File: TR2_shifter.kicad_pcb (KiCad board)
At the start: 2 copper layers, 40 parts, among them J1 Conn_02x07_Odd_Even, J2 Conn_02x07_Odd_Even, U1 LM393DT, U2 LM393DT, U3 LM393DT, U4 LM393DT, U5 LM393DT, U6 LM393DT, U7 LM393DT

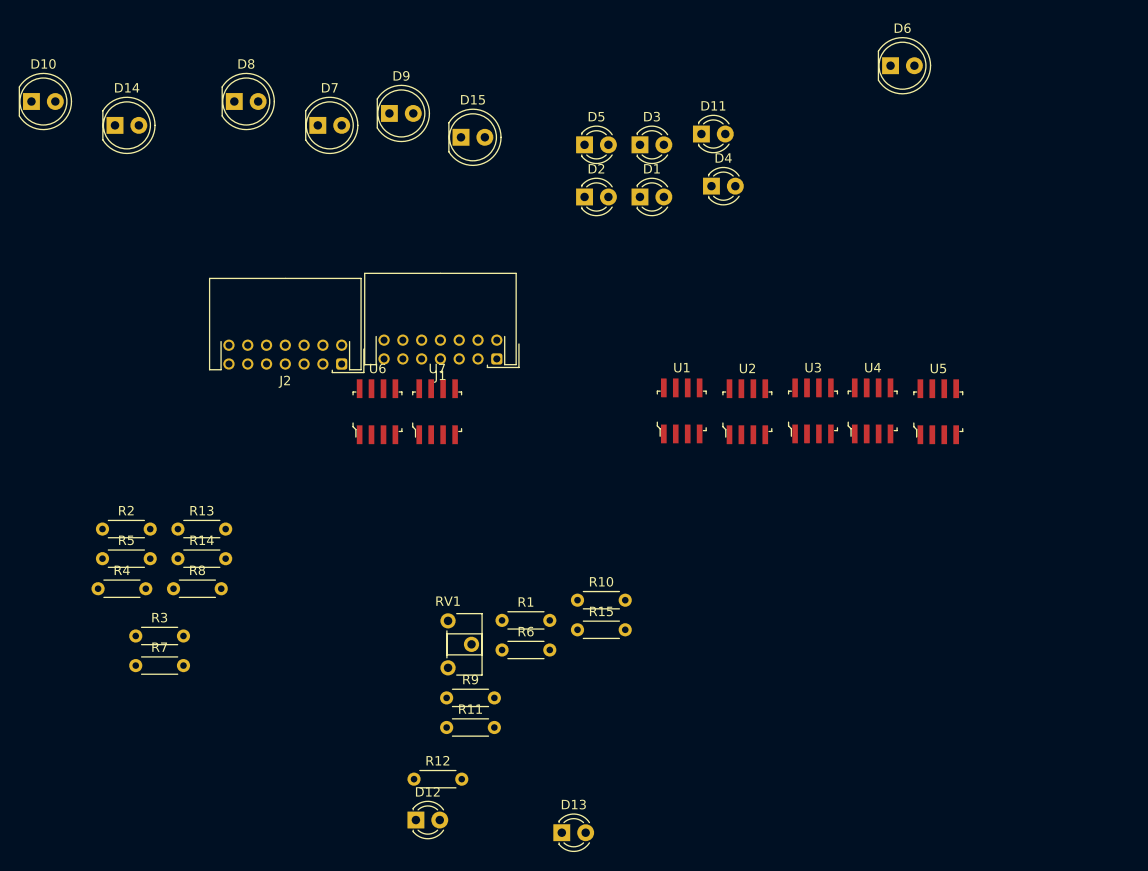
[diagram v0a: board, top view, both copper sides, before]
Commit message: First compact layout - beginning wiring
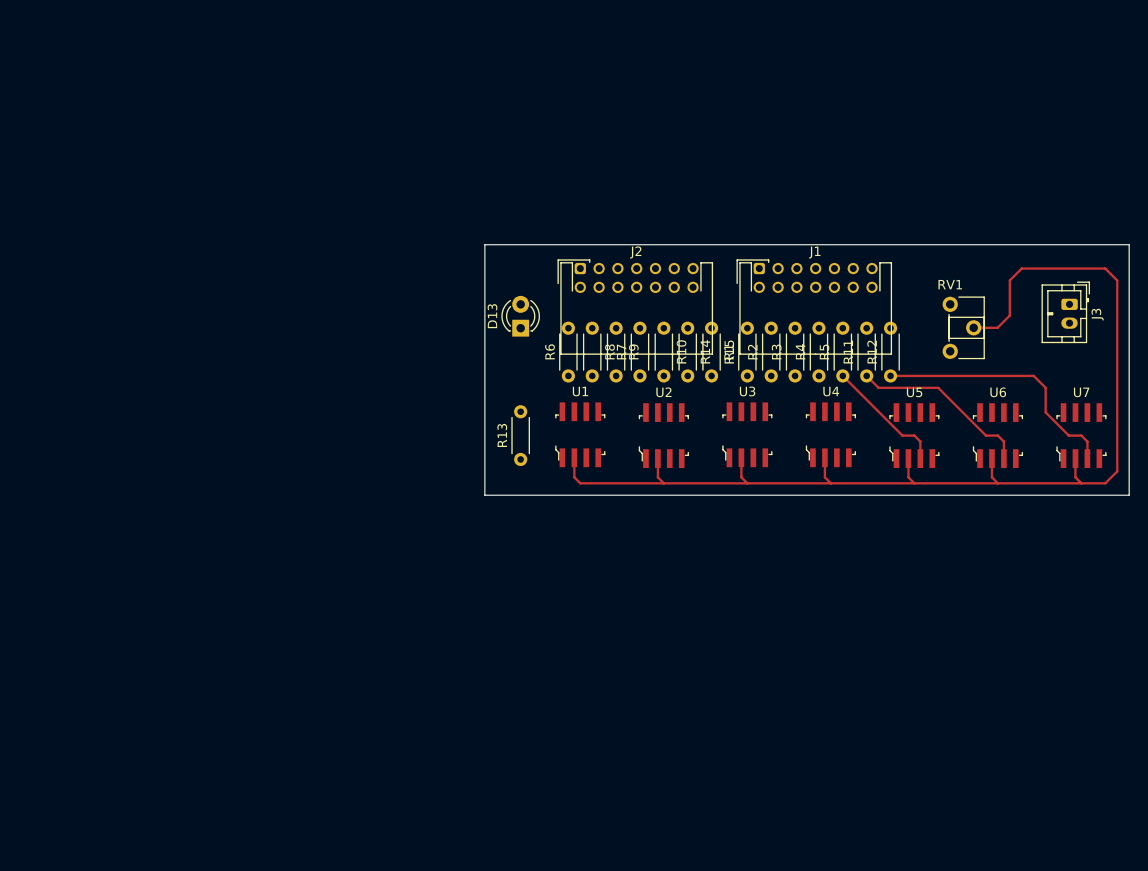
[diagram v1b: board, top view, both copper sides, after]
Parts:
- removed D1, D11, D12, D2, D3, D4, D5: IR RCV, LED_THT:LED_D3.0mm
- removed D10, D14, D15, D9: GREEN LED, LED_THT:LED_D5.0mm
- removed D6, D8: RED LED, LED_THT:LED_D5.0mm
- removed D7: AMBER LED, LED_THT:LED_D5.0mm
- added J3: Conn_01x02, Connector_JST:JST_PH_B2B-PH-K_1x02_P2.00mm_Vertical, F.Cu at (214.6, 74.9)
- moved R5 81.2 mm to (190.5, 82.5), turned to 90 degrees
- moved R4 80.0 mm to (188.0, 82.5), turned to 90 degrees
- moved R3 75.4 mm to (185.4, 82.5), turned to 90 degrees
- moved R2 73.0 mm to (182.9, 82.5), turned to 90 degrees
- moved U7 68.6 mm to (215.9, 88.9)
- moved R12 66.4 mm to (195.6, 82.5), turned to 90 degrees
- moved U6 66.1 mm to (207.0, 88.9)
- moved RV1 63.2 mm to (201.9, 74.9)
- moved R7 61.9 mm to (168.9, 82.5), turned to 90 degrees
- moved R14 59.5 mm to (174.0, 77.5), turned to 270 degrees
- moved R11 58.3 mm to (193.0, 82.5), turned to 90 degrees
- moved D13 53.9 mm to (156.2, 77.5), turned to 90 degrees
- moved R8 52.5 mm to (163.8, 77.5), turned to 270 degrees
- moved R9 43.3 mm to (166.4, 77.5), turned to 270 degrees
- moved R13 37.2 mm to (156.2, 91.4), turned to 90 degrees
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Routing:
- net REF_V: track 0.00 -> 119.1 mm
- net 1_IR: track 0.00 -> 27.2 mm
- net 2_IR: track 0.00 -> 19.3 mm
- net 3_IR: track 0.00 -> 13.0 mm
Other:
- board outline added: 68.6 x 26.7 mm

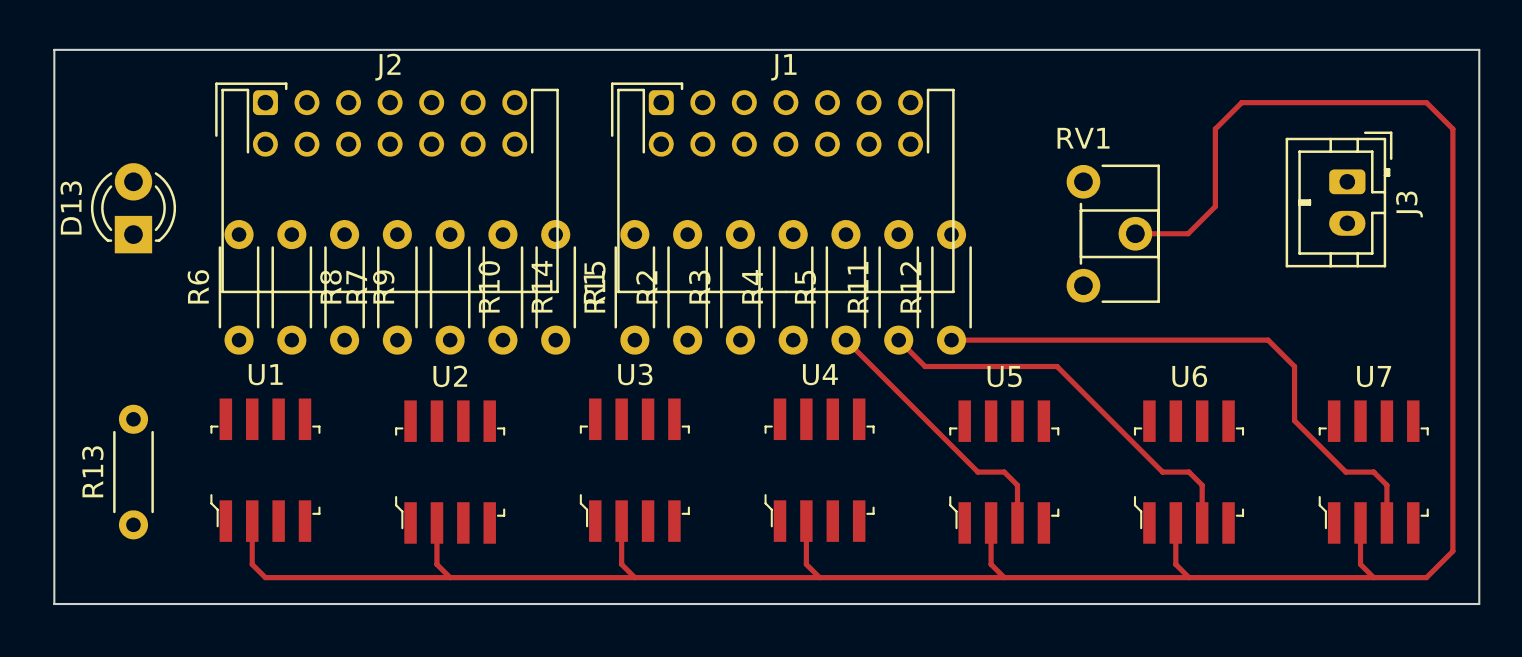
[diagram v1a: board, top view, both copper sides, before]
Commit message: More layout, vias, etc. commiting before swapping LM393 to LM33
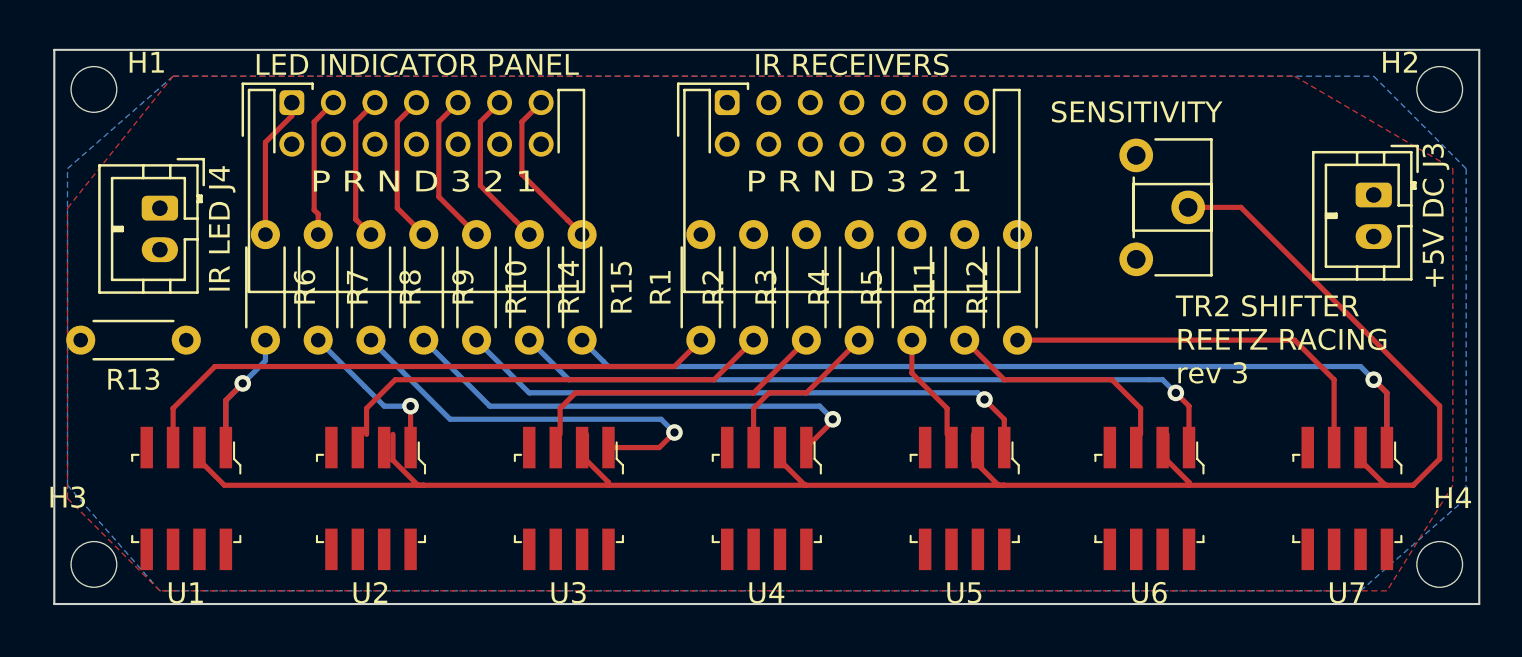
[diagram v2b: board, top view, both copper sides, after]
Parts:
- removed D13: IR Emitter 3mm, LED_THT:LED_D3.0mm_IRBlack
- removed J1: Conn_02x07_Odd_Even, Connector_JST:JST_PHD_S14B-PHDSS_2x07_P2.00mm_Horizontal
- added H1: MountingHole, MountingHole:MountingHole_2.2mm_M2, F.Cu at (154.3, 70.5)
- added H2: MountingHole, MountingHole:MountingHole_2.2mm_M2, F.Cu at (219.1, 70.5)
- added H3: MountingHole, MountingHole:MountingHole_2.2mm_M2, F.Cu at (154.3, 93.3)
- added H4: MountingHole, MountingHole:MountingHole_2.2mm_M2, F.Cu at (219.1, 93.3)
- added IR LED J4: Conn_01x02, Connector_JST:JST_PH_B2B-PH-K_1x02_P2.00mm_Vertical, F.Cu at (157.5, 76.2)
- added IR RECEIVERS: Conn_02x07_Odd_Even, Connector_JST:JST_PHD_S14B-PHDSS_2x07_P2.00mm_Horizontal, F.Cu at (184.8, 71.1)
- +5V DC J3: renamed from J3
- LED INDICATOR PANEL: renamed from J2
- moved R13 9.25 mm to (158.8, 82.5), turned to 180 degrees
- moved R7 6.35 mm to (165.1, 77.5), turned to 270 degrees
- moved R6 5.24 mm to (162.6, 77.5), turned to 270 degrees
- moved U1 4.05 mm to (158.8, 90.2), turned to 180 degrees
- moved U2 4.02 mm to (167.6, 90.2), turned to 180 degrees
- moved R9 3.81 mm to (170.2, 77.5)
- moved R8 3.81 mm to (167.6, 77.5)
- moved U3 3.45 mm to (177.2, 90.2), turned to 180 degrees
- moved R11 3.18 mm to (196.2, 82.5)
- moved R2 3.18 mm to (186.1, 82.5)
- moved R3 3.18 mm to (188.6, 82.5)
- moved R5 3.18 mm to (193.7, 82.5)
- moved R1 3.17 mm to (183.5, 82.5)
- moved R12 3.17 mm to (198.8, 82.5)
- moved R4 3.17 mm to (191.1, 82.5)
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- renumbered RV1 to SENSITIVITY
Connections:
- +5V DC J3 pad 1: +5V -> Net-(J3-Pad1)
- LED INDICATOR PANEL pad 1: +5V -> PARK_INDICATOR
- LED INDICATOR PANEL pad 10: 3_INDICATOR -> +5V
- LED INDICATOR PANEL pad 11: +5V -> 2_INDICATOR
- LED INDICATOR PANEL pad 12: 2_INDICATOR -> +5V
- LED INDICATOR PANEL pad 13: +5V -> 1_INDICATOR
- LED INDICATOR PANEL pad 14: 1_INDICATOR -> +5V
- LED INDICATOR PANEL pad 2: PARK_INDICATOR -> +5V
- LED INDICATOR PANEL pad 3: +5V -> REV_INDICATOR
- LED INDICATOR PANEL pad 4: REV_INDICATOR -> +5V
- LED INDICATOR PANEL pad 5: +5V -> NEU_INDICATOR
- LED INDICATOR PANEL pad 6: NEU_INDICATOR -> +5V
- LED INDICATOR PANEL pad 7: +5V -> DRIVE_INDICATOR
- LED INDICATOR PANEL pad 8: DRIVE_INDICATOR -> +5V
- LED INDICATOR PANEL pad 9: +5V -> 3_INDICATOR
- R13 pad 1: GND -> +5V
- R13 pad 2: Net-(D13-Pad1) -> Net-(J3-Pad1)
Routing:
- net Net-(R15-Pad2): track 0.00 -> 44.6 mm, vias 0 -> 1
- net Net-(R14-Pad2): track 0.00 -> 34.4 mm, vias 0 -> 1
- net PARK_IR: track 0.00 -> 28.0 mm
- net Net-(R10-Pad2): track 0.00 -> 27.7 mm, vias 0 -> 1
- net Net-(R9-Pad2): track 0.00 -> 23.1 mm, vias 0 -> 1
- net REV_IR: track 0.00 -> 21.2 mm
- net REF_V: track 119.1 -> 98.8 mm
- net Net-(R8-Pad2): track 0.00 -> 19.9 mm, vias 0 -> 1
- net NEU_IR: track 0.00 -> 14.5 mm
- net 1_IR: track 27.2 -> 18.7 mm
- net 2_IR: track 19.3 -> 11.1 mm
- net Net-(R6-Pad2): track 0.00 -> 8.02 mm, vias 0 -> 1
- net 1_INDICATOR: track 0.00 -> 7.93 mm
- net Net-(R7-Pad2): track 0.00 -> 7.76 mm, vias 0 -> 1
- net 3_IR: track 13.0 -> 5.24 mm
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- added copper zone on B.Cu, net GND
- added copper zone on F.Cu, net GND
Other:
- board text added: "P R N D 3 2 1"
- board text added: "TR2 SHIFTER REETZ RACING rev 3"

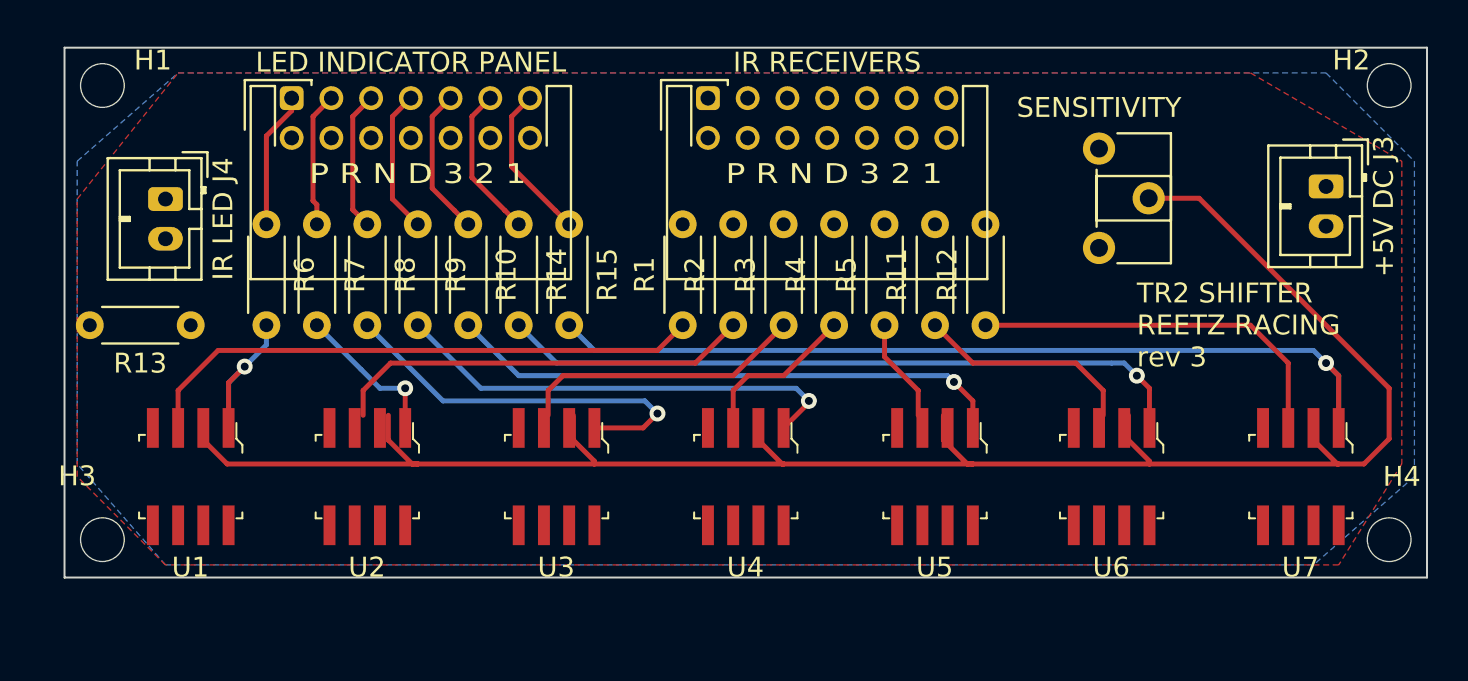
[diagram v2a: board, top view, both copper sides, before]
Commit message: More work on power/ground planes
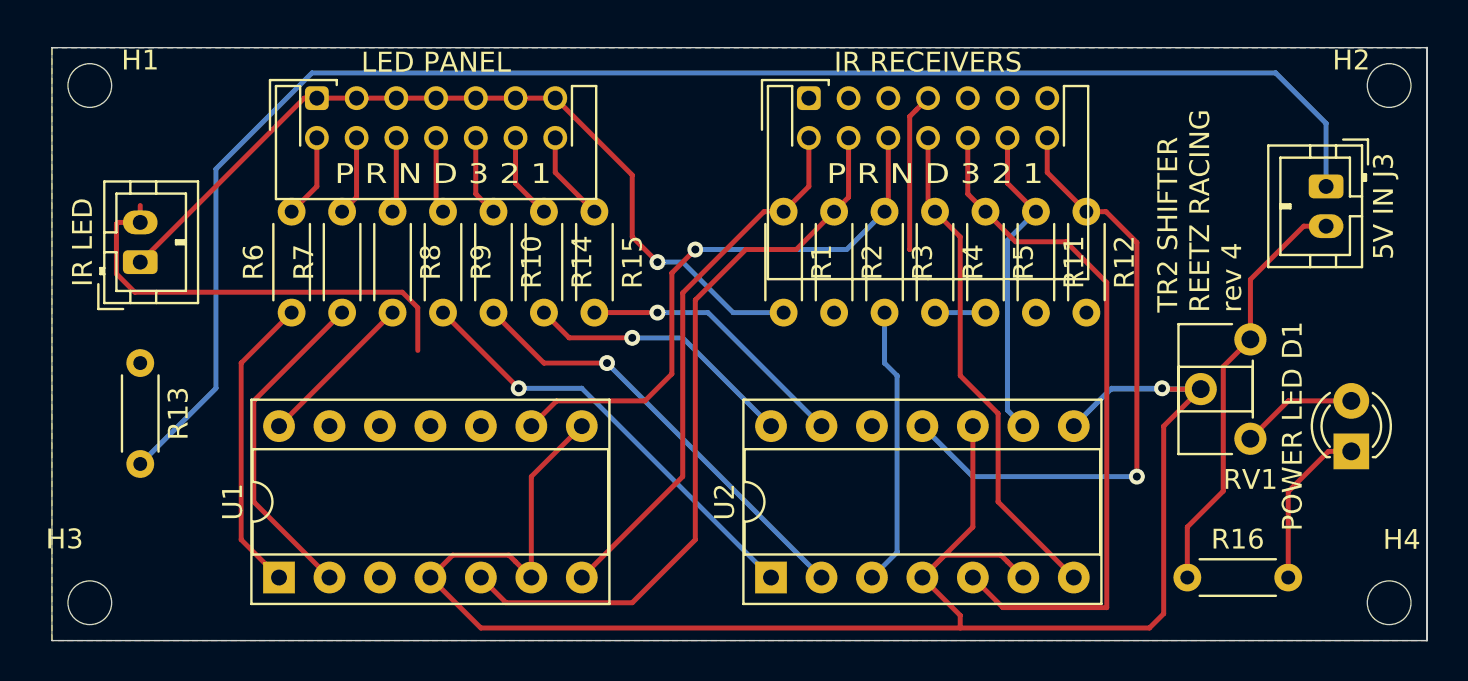
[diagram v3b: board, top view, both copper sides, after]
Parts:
- removed U3, U4, U5, U6, U7: LM393DT, digikey-footprints:SOIC-8_W3.9mm
- added POWER LED D1: POWER ON, LED_THT:LED_D3.0mm, F.Cu at (217.2, 88.9)
- added R16: 22KΩ, Resistor_THT:R_Axial_DIN0204_L3.6mm_D1.6mm_P5.08mm_Horizontal, F.Cu at (208.9, 95.2)
- 5V IN J3: renamed from +5V DC J3
- IR LED: renamed from IR LED J4
- LED PANEL: renamed from LED INDICATOR PANEL
- U1, U2: value LM393DT -> LM339_DIP; footprint digikey-footprints:SOIC-8_W3.9mm -> Package_DIP:DIP-14_W7.62mm_Socket
- moved U2 20.9 mm to (188.0, 95.2), turned to 90 degrees
- moved RV1 16.5 mm to (212.1, 88.3), turned to 180 degrees
- moved R1 7.65 mm to (188.6, 76.8), turned to 270 degrees
- moved R12 7.65 mm to (203.8, 76.8), turned to 270 degrees
- moved R3 7.65 mm to (193.7, 76.8), turned to 270 degrees
- moved R4 7.65 mm to (196.2, 76.8), turned to 270 degrees
- moved R11 7.65 mm to (201.3, 76.8), turned to 270 degrees
- moved R2 7.65 mm to (191.1, 76.8), turned to 270 degrees
- moved R5 7.65 mm to (198.8, 76.8), turned to 270 degrees
- moved U1 6.75 mm to (163.2, 95.2), turned to 90 degrees
- moved IR RECEIVERS 5.08 mm to (189.9, 71.1)
- moved R6 4.62 mm to (163.8, 81.9), turned to 90 degrees
- moved R7 4.62 mm to (166.4, 81.9), turned to 90 degrees
- moved IR LED 3.42 mm to (156.2, 79.4), turned to 90 degrees
- moved H3 3.24 mm to (153.7, 96.5)
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- renumbered SENSITIVITY to RV1
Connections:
- IR RECEIVERS pad 1: PARK_IR -> GND
- IR RECEIVERS pad 10: GND -> 3_IR
- IR RECEIVERS pad 11: 2_IR -> GND
- IR RECEIVERS pad 12: GND -> 2_IR
- IR RECEIVERS pad 13: 1_IR -> GND
- IR RECEIVERS pad 14: GND -> 1_IR
- IR RECEIVERS pad 2: GND -> PARK_IR
- IR RECEIVERS pad 3: REV_IR -> GND
- IR RECEIVERS pad 4: GND -> REV_IR
- IR RECEIVERS pad 5: NEU_IR -> GND
- IR RECEIVERS pad 6: GND -> NEU_IR
- IR RECEIVERS pad 7: DRIVE_IR -> GND
- IR RECEIVERS pad 8: GND -> DRIVE_IR
- IR RECEIVERS pad 9: 3_IR -> GND
- LED PANEL pad 1: PARK_INDICATOR -> +5V
- LED PANEL pad 10: +5V -> 3_INDICATOR
- LED PANEL pad 11: 2_INDICATOR -> +5V
- LED PANEL pad 12: +5V -> 2_INDICATOR
- LED PANEL pad 13: 1_INDICATOR -> +5V
- LED PANEL pad 14: +5V -> 1_INDICATOR
- LED PANEL pad 2: +5V -> PARK_INDICATOR
- LED PANEL pad 3: REV_INDICATOR -> +5V
- LED PANEL pad 4: +5V -> REV_INDICATOR
- LED PANEL pad 5: NEU_INDICATOR -> +5V
- LED PANEL pad 6: +5V -> NEU_INDICATOR
- LED PANEL pad 7: DRIVE_INDICATOR -> +5V
- LED PANEL pad 8: +5V -> DRIVE_INDICATOR
- LED PANEL pad 9: 3_INDICATOR -> +5V
- R6 pad 1: PARK_INDICATOR -> Net-(R6-Pad1)
- R6 pad 2: Net-(R6-Pad2) -> PARK_INDICATOR
- R7 pad 1: REV_INDICATOR -> Net-(R7-Pad1)
- R7 pad 2: Net-(R7-Pad2) -> REV_INDICATOR
- U1 pad 1: Net-(R6-Pad2) -> Net-(R6-Pad1)
- U1 pad 2: REF_V -> Net-(R7-Pad1)
- U1 pad 3: PARK_IR -> +5V
- U1 pad 4: GND -> REF_V
- U1 pad 5: (no net) -> REV_IR
- U1 pad 6: (no net) -> REF_V
- U1 pad 7: (no net) -> PARK_IR
- U1 pad 8: +5V -> REF_V
- U2 pad 1: Net-(R7-Pad2) -> Net-(R9-Pad2)
- U2 pad 2: REF_V -> Net-(R10-Pad2)
- U2 pad 3: REV_IR -> +5V
- U2 pad 4: GND -> REF_V
- U2 pad 5: (no net) -> 3_IR
- U2 pad 6: (no net) -> REF_V
- U2 pad 7: (no net) -> DRIVE_IR
- U2 pad 8: +5V -> REF_V
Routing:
- net Net-(J3-Pad1): track 0.00 -> 78.5 mm
- net +5V: track 0.00 -> 64.6 mm, vias 0 -> 1
- net GND: track 0.00 -> 51.9 mm
- net Net-(R15-Pad2): track 44.6 -> 13.8 mm
- net 3_IR: track 5.24 -> 35.4 mm
- net Net-(R14-Pad2): track 34.4 -> 13.8 mm
- net DRIVE_IR: track 7.69 -> 25.2 mm
- net Net-(R7-Pad1): track 0.00 -> 16.8 mm
- net REV_IR: track 21.2 -> 37.5 mm
- net Net-(R6-Pad1): track 0.00 -> 15.2 mm
- net NEU_IR: track 14.5 -> 29.0 mm, vias 0 -> 1
- net 1_IR: track 18.7 -> 31.3 mm, vias 0 -> 1
- net Net-(R8-Pad2): track 19.9 -> 8.08 mm, vias 1 -> 0
- net Net-(D1-Pad1): track 0.00 -> 8.34 mm
- net Net-(R6-Pad2): track 8.02 -> 0.00 mm, vias 1 -> 0
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- added copper zone on B.Cu, net +5V
- removed copper zone on B.Cu, net GND
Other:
- board size 68.6 x 26.7 mm -> 69.2 x 29.8 mm
- board text added: "TR2 SHIFTER REETZ RACING rev 4"
- board text removed: "TR2 SHIFTER REETZ RACING rev 3"
